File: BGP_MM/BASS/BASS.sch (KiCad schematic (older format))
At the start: 8 parts, among them J1 Conn_01x02_Male, J2 Conn_01x02_Male, J3 Conn_01x04_Male, J4 Conn_01x04_Male, P2 Conn_01x02, P3 Conn_01x02, P4 Conn_01x03

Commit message: Board Labels
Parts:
- RV1: symbol POT -> POT-RESCUE-BASS
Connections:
- net Earth: now also P2.1 (Pin_1), P3.1 (Pin_1), P4.1 (Pin_1); no longer P2.2 (Pin_2), P3.2 (Pin_2), P4.3 (Pin_3)
- net JZ_I: now also P2.2 (Pin_2); no longer P2.1 (Pin_1)
- net MM_BH: now also P4.3 (Pin_3); no longer P4.1 (Pin_1)
- net MM_NH: now also P3.2 (Pin_2); no longer P3.1 (Pin_1)
- net at J1.1 (Pin_1): now also RV1.2; no longer RV1.1
- net at J1.2 (Pin_2): now also RV1.3; no longer RV1.2
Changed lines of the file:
@@
 EESchema Schematic File Version 2
+LIBS:BASS-rescue
 LIBS:power
 LIBS:device
@@
 LIBS:contrib
 LIBS:valves
+LIBS:BASS-cache
 EELAYER 25 0
 EELAYER END
@@
 Text Label 7500 3550 0    60   ~ 0
 JZ_I
-Text Label 8400 4150 0    60   ~ 0
+Text Label 8400 4350 0    60   ~ 0
 MM_BH
 Text Label 8400 4250 0    60   ~ 0
 MM_BC
+Text Label 8400 3900 0    60   ~ 0
+MM_NH
 Text Label 8400 3800 0    60   ~ 0
-MM_NH
-Text Label 8400 3900 0    60   ~ 0
 MM_NC
-Text Label 8400 3450 0    60   ~ 0
+Text Label 8400 3550 0    60   ~ 0
 JZ_I
 $Comp
 L Earth #PWR02
 U 1 1 5B02DBB9
-P 8400 3550
-F 0 "#PWR02" H 8400 3300 50  0001 C CNN
-F 1 "Earth" H 8400 3400 50  0001 C CNN
-F 2 "" H 8400 3550 50  0001 C CNN
-F 3 "" H 8400 3550 50  0001 C CNN
-	1    8400 3550
-	1    0    0    -1
+P 8400 3450
+F 0 "#PWR02" H 8400 3200 50  0001 C CNN
+F 1 "Earth" H 8400 3300 50  0001 C CNN
+F 2 "" H 8400 3450 50  0001 C CNN
+F 3 "" H 8400 3450 50  0001 C CNN
+	1    8400 3450
+	0    -1   -1   0
 $EndComp
 $Comp
@@
 L Earth #PWR05
 U 1 1 5B04DD41
-P 8400 4350
-F 0 "#PWR05" H 8400 4100 50  0001 C CNN
-F 1 "Earth" H 8400 4200 50  0001 C CNN
-F 2 "" H 8400 4350 50  0001 C CNN
-F 3 "" H 8400 4350 50  0001 C CNN
-	1    8400 4350
-	1    0    0    -1
+P 8400 4150
+F 0 "#PWR05" H 8400 3900 50  0001 C CNN
+F 1 "Earth" H 8400 4000 50  0001 C CNN
+F 2 "" H 8400 4150 50  0001 C CNN
+F 3 "" H 8400 4150 50  0001 C CNN
+	1    8400 4150
+	0    -1   -1   0
 $EndComp
 $Comp
 L Conn_01x02_Male J1
 U 1 1 5B08BD93
-P 4900 3450
-F 0 "J1" H 4900 3550 50  0000 C CNN
-F 1 "Conn_01x02_Male" H 4900 3250 50  0001 C CNN
-F 2 "Connectors_JST:JST_PH_B2B-PH-K_02x2.00mm_Straight" H 4900 3450 50  0001 C CNN
-F 3 "" H 4900 3450 50  0001 C CNN
-	1    4900 3450
-	1    0    0    -1
-$EndComp
-$Comp
-L POT RV1
+P 4900 3550
+F 0 "J1" H 4900 3350 50  0000 C CNN
+F 1 "Conn_01x02_Male" H 4900 3350 50  0001 C CNN
+F 2 "Connectors_JST:JST_PH_B2B-PH-K_02x2.00mm_Straight" H 4900 3550 50  0001 C CNN
+F 3 "" H 4900 3550 50  0001 C CNN
+	1    4900 3550
+	1    0    0    1
+$EndComp
+$Comp
+L POT-RESCUE-BASS RV1
 U 1 1 5B08BE8C
 P 5350 3600
@@
 F 3 "" H 5350 3600 50  0001 C CNN
 	1    5350 3600
-	-1   0    0    -1
+	-1   0    0    1
 $EndComp
 Wire Wire Line

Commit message: MM Gerbers, BASS pot fixup
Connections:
- net at J1.1 (Pin_1): now also RV1.1; no longer RV1.2
- net at J1.2 (Pin_2): now also RV1.2; no longer RV1.3
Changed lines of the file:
@@
 L Conn_01x02_Male J1
 U 1 1 5B08BD93
-P 4900 3550
-F 0 "J1" H 4900 3350 50  0000 C CNN
-F 1 "Conn_01x02_Male" H 4900 3350 50  0001 C CNN
-F 2 "Connectors_JST:JST_PH_B2B-PH-K_02x2.00mm_Straight" H 4900 3550 50  0001 C CNN
-F 3 "" H 4900 3550 50  0001 C CNN
-	1    4900 3550
-	1    0    0    1
+P 4900 3450
+F 0 "J1" H 4900 3550 50  0000 C CNN
+F 1 "Conn_01x02_Male" H 4900 3250 50  0001 C CNN
+F 2 "Connectors_JST:JST_PH_B2B-PH-K_02x2.00mm_Straight" H 4900 3450 50  0001 C CNN
+F 3 "" H 4900 3450 50  0001 C CNN
+	1    4900 3450
+	1    0    0    -1
 $EndComp
 $Comp
@@
 F 3 "" H 5350 3600 50  0001 C CNN
 	1    5350 3600
-	-1   0    0    1
+	-1   0    0    -1
 $EndComp
 Wire Wire Line

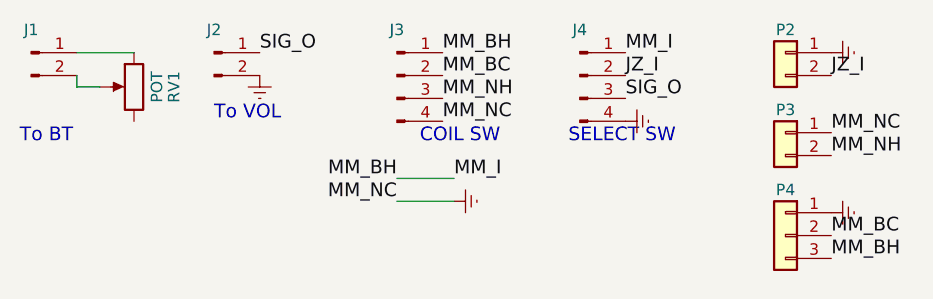
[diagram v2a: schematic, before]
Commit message: MM Switch Config Changed
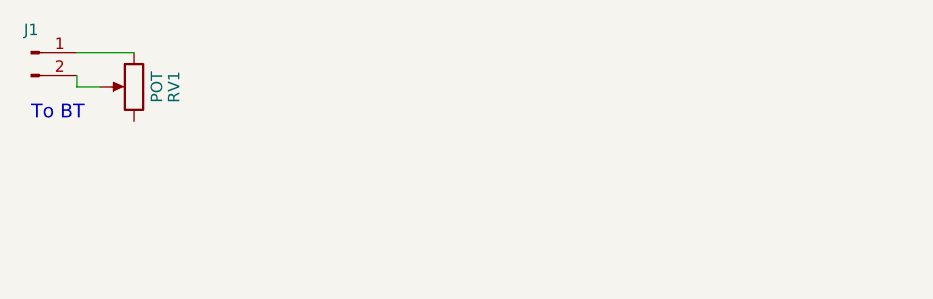
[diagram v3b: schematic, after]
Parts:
- removed J2: Conn_01x02_Male, Connectors_JST:JST_PH_B2B-PH-K_02x2.00mm_Straight, symbol Conn_01x02_Male
- removed J3, J4: Conn_01x04_Male, Connectors_JST:JST_PH_B4B-PH-K_04x2.00mm_Straight, symbol Conn_01x04_Male
- removed P2, P3: Conn_01x02, LIBS:TerminalBlock_Phoenix_MPT-2.54mm_2pol, symbol Conn_01x02
- removed P4: Conn_01x03, LIBS:TerminalBlock_Phoenix_MPT-2.54mm_3pol, symbol Conn_01x03
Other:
- note removed: "COIL SW"
- note removed: "SELECT SW"
- note removed: "To VOL"
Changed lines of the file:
@@
 Comment4 ""
 $EndDescr
-Text Notes 5700 3750 0    60   ~ 0
-To VOL
-Text Notes 4850 3850 0    60   ~ 0
+Text Notes 4900 3750 0    60   ~ 0
 To BT
-$Comp
-L Earth #PWR01
-U 1 1 5B02D550
-P 5900 3550
-F 0 "#PWR01" H 5900 3300 50  0001 C CNN
-F 1 "Earth" H 5900 3400 50  0001 C CNN
-F 2 "" H 5900 3550 50  0001 C CNN
-F 3 "" H 5900 3550 50  0001 C CNN
-	1    5900 3550
-	1    0    0    -1
-$EndComp
-Text Label 5900 3450 0    60   ~ 0
-SIG_O
-Text Notes 6600 3850 0    60   ~ 0
-COIL SW
-Text Notes 7250 3850 0    60   ~ 0
-SELECT SW
-Text Label 6700 3450 0    60   ~ 0
-MM_BH
-Text Label 6700 3550 0    60   ~ 0
-MM_BC
-Text Label 6700 3750 0    60   ~ 0
-MM_NC
-Text Label 6700 3650 0    60   ~ 0
-MM_NH
-Text Label 7500 3450 0    60   ~ 0
-MM_I
-Text Label 7500 3550 0    60   ~ 0
-JZ_I
-Text Label 8400 4350 0    60   ~ 0
-MM_BH
-Text Label 8400 4250 0    60   ~ 0
-MM_BC
-Text Label 8400 3900 0    60   ~ 0
-MM_NH
-Text Label 8400 3800 0    60   ~ 0
-MM_NC
-Text Label 8400 3550 0    60   ~ 0
-JZ_I
-$Comp
-L Earth #PWR02
-U 1 1 5B02DBB9
-P 8400 3450
-F 0 "#PWR02" H 8400 3200 50  0001 C CNN
-F 1 "Earth" H 8400 3300 50  0001 C CNN
-F 2 "" H 8400 3450 50  0001 C CNN
-F 3 "" H 8400 3450 50  0001 C CNN
-	1    8400 3450
-	0    -1   -1   0
-$EndComp
-$Comp
-L Earth #PWR03
-U 1 1 5B02DBEB
-P 6750 4100
-F 0 "#PWR03" H 6750 3850 50  0001 C CNN
-F 1 "Earth" H 6750 3950 50  0001 C CNN
-F 2 "" H 6750 4100 50  0001 C CNN
-F 3 "" H 6750 4100 50  0001 C CNN
-	1    6750 4100
-	0    -1   -1   0
-$EndComp
-$Comp
-L Conn_01x04_Male J3
-U 1 1 5B03DCFD
-P 6500 3550
-F 0 "J3" H 6500 3750 50  0000 C CNN
-F 1 "Conn_01x04_Male" H 6500 3250 50  0001 C CNN
-F 2 "Connectors_JST:JST_PH_B4B-PH-K_04x2.00mm_Straight" H 6500 3550 50  0001 C CNN
-F 3 "" H 6500 3550 50  0001 C CNN
-	1    6500 3550
-	1    0    0    -1
-$EndComp
-$Comp
-L Conn_01x04_Male J4
-U 1 1 5B03DD3B
-P 7300 3550
-F 0 "J4" H 7300 3750 50  0000 C CNN
-F 1 "Conn_01x04_Male" H 7300 3250 50  0001 C CNN
-F 2 "Connectors_JST:JST_PH_B4B-PH-K_04x2.00mm_Straight" H 7300 3550 50  0001 C CNN
-F 3 "" H 7300 3550 50  0001 C CNN
-	1    7300 3550
-	1    0    0    -1
-$EndComp
-$Comp
-L Conn_01x02_Male J2
-U 1 1 5B03DF38
-P 5700 3450
-F 0 "J2" H 5700 3550 50  0000 C CNN
-F 1 "Conn_01x02_Male" H 5700 3250 50  0001 C CNN
-F 2 "Connectors_JST:JST_PH_B2B-PH-K_02x2.00mm_Straight" H 5700 3450 50  0001 C CNN
-F 3 "" H 5700 3450 50  0001 C CNN
-	1    5700 3450
-	1    0    0    -1
-$EndComp
-Text Label 6750 4000 0    60   ~ 0
-MM_I
-Wire Wire Line
-	6500 4000 6750 4000
-Text Label 6500 4000 2    60   ~ 0
-MM_BH
-Wire Wire Line
-	6750 4100 6500 4100
-Text Label 7500 3650 0    60   ~ 0
-SIG_O
-$Comp
-L Earth #PWR04
-U 1 1 5B04B257
-P 7500 3750
-F 0 "#PWR04" H 7500 3500 50  0001 C CNN
-F 1 "Earth" H 7500 3600 50  0001 C CNN
-F 2 "" H 7500 3750 50  0001 C CNN
-F 3 "" H 7500 3750 50  0001 C CNN
-	1    7500 3750
-	0    -1   -1   0
-$EndComp
-Text Label 6500 4100 2    60   ~ 0
-MM_NC
-$Comp
-L Earth #PWR05
-U 1 1 5B04DD41
-P 8400 4150
-F 0 "#PWR05" H 8400 3900 50  0001 C CNN
-F 1 "Earth" H 8400 4000 50  0001 C CNN
-F 2 "" H 8400 4150 50  0001 C CNN
-F 3 "" H 8400 4150 50  0001 C CNN
-	1    8400 4150
-	0    -1   -1   0
-$EndComp
 $Comp
 L Conn_01x02_Male J1
@@
 Wire Wire Line
 	5100 3450 5350 3450
-$Comp
-L Conn_01x02 P2
-U 1 1 5B08BF2B
-P 8200 3450
-F 0 "P2" H 8200 3550 50  0000 C CNN
-F 1 "Conn_01x02" H 8200 3250 50  0001 C CNN
-F 2 "LIBS:TerminalBlock_Phoenix_MPT-2.54mm_2pol" H 8200 3450 50  0001 C CNN
-F 3 "" H 8200 3450 50  0001 C CNN
-	1    8200 3450
-	-1   0    0    -1
-$EndComp
-$Comp
-L Conn_01x02 P3
-U 1 1 5B08BF5E
-P 8200 3800
-F 0 "P3" H 8200 3900 50  0000 C CNN
-F 1 "Conn_01x02" H 8200 3600 50  0001 C CNN
-F 2 "LIBS:TerminalBlock_Phoenix_MPT-2.54mm_2pol" H 8200 3800 50  0001 C CNN
-F 3 "" H 8200 3800 50  0001 C CNN
-	1    8200 3800
-	-1   0    0    -1
-$EndComp
-$Comp
-L Conn_01x03 P4
-U 1 1 5B08BF82
-P 8200 4250
-F 0 "P4" H 8200 4450 50  0000 C CNN
-F 1 "Conn_01x03" H 8200 4050 50  0001 C CNN
-F 2 "LIBS:TerminalBlock_Phoenix_MPT-2.54mm_3pol" H 8200 4250 50  0001 C CNN
-F 3 "" H 8200 4250 50  0001 C CNN
-	1    8200 4250
-	-1   0    0    -1
-$EndComp
 $EndSCHEMATC

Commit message: MM Refactoring
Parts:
- J1: footprint Connectors_JST:JST_PH_B2B-PH-K_02x2.00mm_Straight -> Pin_Headers:Pin_Header_Straight_2x01_Pitch2.54mm
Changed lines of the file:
@@
 F 0 "J1" H 4900 3550 50  0000 C CNN
 F 1 "Conn_01x02_Male" H 4900 3250 50  0001 C CNN
-F 2 "Connectors_JST:JST_PH_B2B-PH-K_02x2.00mm_Straight" H 4900 3450 50  0001 C CNN
+F 2 "Pin_Headers:Pin_Header_Straight_2x01_Pitch2.54mm" H 4900 3450 50  0001 C CNN
 F 3 "" H 4900 3450 50  0001 C CNN
 	1    4900 3450
